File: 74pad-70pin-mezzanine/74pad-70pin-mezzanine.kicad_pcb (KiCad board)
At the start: 4 copper layers, 14 x 16 mm, 11 parts

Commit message: fix and add project code areas to panel
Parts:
- C101, C102, C103, C104, C105, C106, C107, C108: value C_Small -> 1 uF
- U101: footprint Connector_Mezzanine:CONN-SMD_70P-P0.40_HCTL_HC-PBB40C-70DP-0.4V-02 -> Connector:CONN-SMD_70P-P0.40_HCTL_HC-PBB40C-70DP-0.4V-02
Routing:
- net PWR_AUX_1: track 4.17 -> 8.81 mm, vias 0 -> 1
- net GND: vias 33 -> 34
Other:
- board outline removed

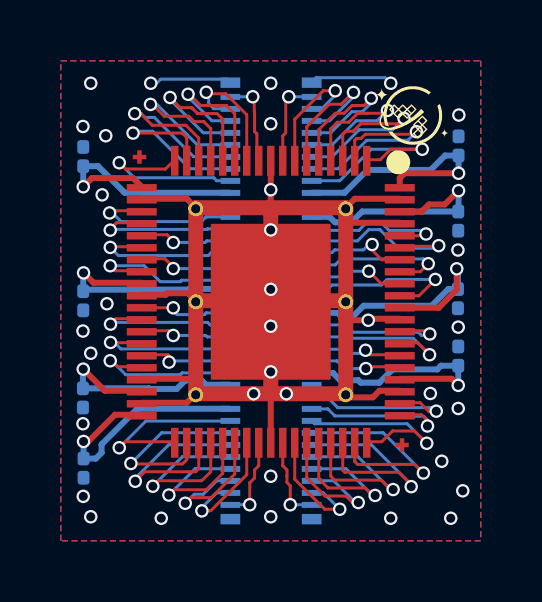
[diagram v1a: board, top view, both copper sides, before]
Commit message: fix edgecuts on panel
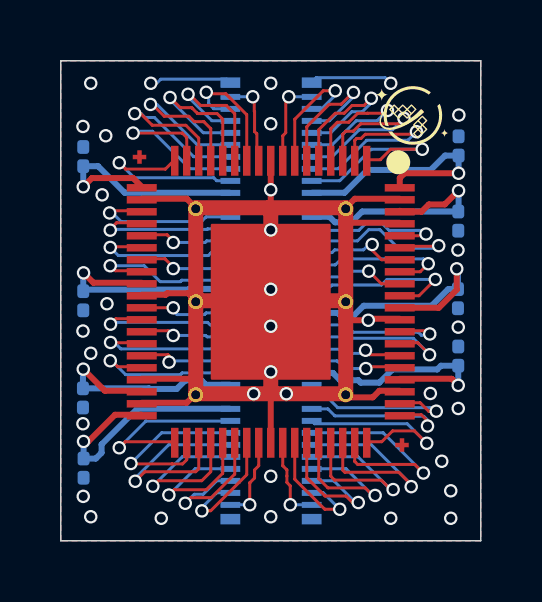
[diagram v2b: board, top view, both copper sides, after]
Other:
- board outline added: 14 x 16 mm
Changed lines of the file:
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@@
 		)
 		(fill no)
-		(layer "User.4")
+		(layer "Edge.Cuts")
 	)
 	(gr_text "70 PIN MEZZANINE\n74 PIN PADRING\nVERSION: TT01"
@@
 	)
 	(via
-		(at 175.22 91.49)
-		(size 0.45)
-		(drill 0.3)
+		(at 174.82 91.49)
+		(size 0.45)
+		(drill 0.3)
